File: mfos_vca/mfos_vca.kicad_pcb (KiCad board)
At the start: 2 copper layers, 236.8 x 141.5 mm, 89 parts, among them J1 CV1 A, J2 CV2 A, J3 Signal In A, J4 Signal Out A, J5 CV1 B, J6 CV2 B, J7 Signal In B, J8 Signal Out A, J9 Conn_02x05_Odd_Even, Q1 2N3904, Q2 2N3906, Q3 2N3904, Q4 2N3906, SW1 SW_SPDT, SW2 SW_SPDT, U1 TL074, U2 LM13700

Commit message: Remove secondary CV input per VCA, some more panel progress
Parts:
- J1: renamed from J2; footprint Connector_PinHeader_2.54mm:PinHeader_1x03_P2.54mm_Vertical_AudioJack -> Connector_PinHeader_2.54mm:PinHeader_1x03_P2.54mm_Vertical
- J2: renamed from J3; footprint Connector_PinHeader_2.54mm:PinHeader_1x03_P2.54mm_Vertical_AudioJack -> Connector_PinHeader_2.54mm:PinHeader_1x03_P2.54mm_Vertical
- J3: renamed from J4; footprint Connector_PinHeader_2.54mm:PinHeader_1x03_P2.54mm_Vertical_AudioJack -> Connector_PinHeader_2.54mm:PinHeader_1x03_P2.54mm_Vertical
- J4: renamed from J6; footprint Connector_PinHeader_2.54mm:PinHeader_1x03_P2.54mm_Vertical_AudioJack -> Connector_PinHeader_2.54mm:PinHeader_1x03_P2.54mm_Vertical
- J5: renamed from J7; footprint Connector_PinHeader_2.54mm:PinHeader_1x03_P2.54mm_Vertical_AudioJack -> Connector_PinHeader_2.54mm:PinHeader_1x03_P2.54mm_Vertical
- J6: renamed from J8; footprint Connector_PinHeader_2.54mm:PinHeader_1x03_P2.54mm_Vertical_AudioJack -> Connector_PinHeader_2.54mm:PinHeader_1x03_P2.54mm_Vertical
- J7: renamed from J9; moved to B.Cu
- moved J7 140.9 mm to (275.5, 129.5), turned to 180 degrees
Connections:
- R13 pad 1: Net-(J3-PadT) -> Net-(J2-PadT)
- R19 pad 2: Net-(J4-PadT) -> Net-(J3-PadT)
- R2 pad 1: Net-(J2-PadT) -> Net-(J1-PadT)
- R20 pad 1: Net-(J6-PadT) -> Net-(J4-PadT)
- R24 pad 1: Net-(J7-PadT) -> Net-(J5-PadT)
- R38 pad 2: Net-(J8-PadT) -> Net-(J6-PadT)
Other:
- outline, holes or cut-outs redrawn
- board text added: "CV"
- board text added: "IN"
- board text added: "LIN"
- board text added: "LOG"
- board text added: "OFFSET"
- board text added: "OUT"
- board text removed: "OFFSET A"

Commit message: More progress, got rid of second cv input
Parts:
- removed the J1 at (30.0, 65.0)
- removed the J1 at (29.0, 83.0)
- removed R1: 100k, Resistor_THT:R_Axial_DIN0207_L6.3mm_D2.5mm_P10.16mm_Horizontal
- added J1: CV A, Library:PinHeader_1x03_P2.54mm_Vertical_AudioJack, F.Cu at (244.4, 76.4)
- added REF**: MountingHole_3.2mm_M3, MountingHole:MountingHole_3.2mm_M3, F.Cu at (212.5, 147.5)
- added REF**: MountingHole_3.2mm_M3, MountingHole:MountingHole_3.2mm_M3, F.Cu at (212.5, 36.0)
- added REF**: MountingHole_3.2mm_M3, MountingHole:MountingHole_3.2mm_M3, F.Cu at (333.9, 150.0)
- added REF**: MountingHole_3.2mm_M3, MountingHole:MountingHole_3.2mm_M3, F.Cu at (308.5, 150.0)
- added REF**: MountingHole_3.2mm_M3, MountingHole:MountingHole_3.2mm_M3, F.Cu at (308.5, 49.5)
- added REF**: MountingHole_3.2mm_M3, MountingHole:MountingHole_3.2mm_M3, F.Cu at (212.5, 158.5)
- added REF**: MountingHole_3.2mm_M3, MountingHole:MountingHole_3.2mm_M3, F.Cu at (212.5, 47.0)
- added REF**: MountingHole_3.2mm_M3, MountingHole:MountingHole_3.2mm_M3, F.Cu at (333.9, 49.5)
- J2, J3, J5: footprint Connector_PinHeader_2.54mm:PinHeader_1x03_P2.54mm_Vertical -> Library:PinHeader_1x03_P2.54mm_Vertical_AudioJack
- J4: value CV2 B -> CV B; footprint Connector_PinHeader_2.54mm:PinHeader_1x03_P2.54mm_Vertical -> Library:PinHeader_1x03_P2.54mm_Vertical_AudioJack
- J6: value Signal Out A -> Signal Out B; footprint Connector_PinHeader_2.54mm:PinHeader_1x03_P2.54mm_Vertical -> Library:PinHeader_1x03_P2.54mm_Vertical_AudioJack
- RV2, RV3: moved to B.Cu
- moved REF** 268.2 mm to (201.8, -133.0)
- moved REF** 268.2 mm to (201.8, -122.0)
- moved REF** 268.2 mm to (201.8, -10.5)
- moved REF** 268.2 mm to (201.8, -21.5)
- moved REF** 268.2 mm to (176.4, -10.5)
- moved REF** 268.2 mm to (176.4, -133.0)
- moved REF** 268.2 mm to (176.4, -122.0)
- moved REF** 268.2 mm to (176.4, -21.5)
- moved J3 244.3 mm to (287.5, 66.5)
- moved U2 215.3 mm to (257.0, 101.0), turned to 90 degrees
- moved J2 211.7 mm to (244.4, 66.0)
- moved R4 211.0 mm to (247.8, 63.5)
- moved R2 210.8 mm to (247.8, 59.5)
- moved SW1 210.5 mm to (287.5, 55.9)
- moved R3 203.2 mm to (247.9, 55.0)
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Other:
- board size 236.8 x 141.5 mm -> 196.4 x 297.5 mm

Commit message: vca pcb progress from last night
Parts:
- moved R2 19.4 mm to (258.8, 43.5)
- moved R12 18.1 mm to (272.0, 58.5), turned to 90 degrees
- moved R7 13.1 mm to (252.0, 58.7), turned to 90 degrees
- moved R6 13.0 mm to (248.0, 58.5), turned to 90 degrees
- moved R11 13.0 mm to (268.0, 58.5), turned to 90 degrees
- moved R3 11.9 mm to (244.8, 43.5)
- moved C1 10.1 mm to (244.5, 138.5)
- moved C2 10.1 mm to (244.5, 129.0)
- moved C3 10.1 mm to (243.5, 121.5)
- moved C4 10.1 mm to (243.5, 116.0)
- moved D1 10.1 mm to (267.5, 141.0)
- moved D2 10.1 mm to (263.0, 133.4)
- moved J1 10.1 mm to (235.9, 70.9)
- moved J3 10.1 mm to (279.0, 61.0)
- moved J7 10.1 mm to (277.0, 123.8)
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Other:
- outline, holes or cut-outs redrawn

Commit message: Finished placing components on vca board
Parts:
- removed the J4 at (114.2, 97.2)
- removed the REF** at (333.9, 150.0)
- removed the REF** at (308.5, 150.0)
- removed the REF** at (308.5, 49.5)
- removed the REF** at (333.9, 49.5)
- J4: renamed from J5; value CV1 B -> CV B
- RV5, RV6: moved to B.Cu
- moved R27 159.4 mm to (269.1, 116.7), turned to 90 degrees
- moved R26 156.8 mm to (265.1, 116.7), turned to 90 degrees
- moved R25 154.4 mm to (261.1, 116.7), turned to 90 degrees
- moved R37 153.5 mm to (268.9, 131.2), turned to 90 degrees
- moved R36 151.7 mm to (264.8, 131.2), turned to 90 degrees
- moved R24 151.4 mm to (257.0, 114.7), turned to 90 degrees
- moved R38 151.2 mm to (274.5, 114.7), turned to 90 degrees
- moved R35 150.1 mm to (260.8, 131.2), turned to 90 degrees
- moved R23 149.4 mm to (252.9, 114.7), turned to 90 degrees
- moved R34 147.2 mm to (256.7, 128.2), turned to 90 degrees
- moved R22 146.7 mm to (249.0, 114.7), turned to 90 degrees
- moved R28 146.5 mm to (260.5, 103.0)
- moved J6 144.8 mm to (279.0, 104.4)
- moved R21 143.4 mm to (245.0, 114.5), turned to 90 degrees
- moved R20 140.3 mm to (241.0, 114.5), turned to 90 degrees
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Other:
- board size 196.4 x 297.5 mm -> 168.8 x 292 mm

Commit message: Almost done all of the tracks in vca pcb, fix the custom library footprint
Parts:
- removed the REF** at (176.4, -133.0)
- removed the REF** at (176.4, -122.0)
- removed the REF** at (201.8, -122.0)
- removed the REF** at (201.8, -10.5)
- removed the REF** at (201.8, -21.5)
- removed the REF** at (176.4, -21.5)
- removed the REF** at (201.8, -133.0)
- removed the REF** at (176.4, -10.5)
- J1, J2, J3, J5, J6: footprint Library:PinHeader_1x03_P2.54mm_Vertical_AudioJack -> CustomStuff:PinHeader_1x03_P2.54mm_Vertical_AudioJack
- J4: footprint Connector_PinHeader_2.54mm:PinHeader_1x03_P2.54mm_Vertical_AudioJack -> CustomStuff:PinHeader_1x03_P2.54mm_Vertical_AudioJack
- moved Q3 46.5 mm to (219.6, 97.2)
- moved Q4 46.5 mm to (226.1, 97.2)
- moved C7 45.2 mm to (236.1, 90.7)
- moved Q2 42.8 mm to (233.6, 97.2)
- moved R3 40.0 mm to (201.6, 61.7)
- moved R13 40.0 mm to (201.6, 64.6)
- moved R6 40.0 mm to (209.6, 61.6)
- moved R15 40.0 mm to (205.6, 74.7)
- moved R16 40.0 mm to (209.6, 74.7)
- moved R5 40.0 mm to (205.7, 61.7)
- moved RV6 39.6 mm to (214.6, 101.7), turned to -90 degrees
- moved J4 39.1 mm to (197.0, 101.0)
- moved R4 39.1 mm to (214.7, 61.7)
- moved C2 39.1 mm to (207.1, 136.7)
- moved C8 39.1 mm to (221.6, 90.7)
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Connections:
- J4 pad T: Net-(J5-PadT) -> Net-(J4-PadT)
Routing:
- net -12V: track 0.00 -> 286.3 mm
- net +12V: track 0.00 -> 259.6 mm
- net Net-(R25-Pad2): track 0.00 -> 90.6 mm, vias 0 -> 1
- net Net-(U1C--): track 0.00 -> 84.3 mm, vias 0 -> 2
- net Net-(Q1-B): track 0.00 -> 82.2 mm, vias 0 -> 3
- net Net-(Q3-B): track 0.00 -> 67.1 mm, vias 0 -> 3
- net Net-(U1C-+): track 0.00 -> 62.2 mm, vias 0 -> 1
- net GND: track 0.00 -> 61.5 mm, vias 0 -> 4
- net Net-(Q3-E): track 0.00 -> 57.7 mm, vias 0 -> 2
- net Net-(U1D--): track 0.00 -> 54.6 mm, vias 0 -> 2
- net Net-(R36-Pad2): track 0.00 -> 53.1 mm, vias 0 -> 1
- net Net-(R37-Pad2): track 0.00 -> 52.6 mm, vias 0 -> 1
- net Net-(U1D-+): track 0.00 -> 51.5 mm, vias 0 -> 1
- net Net-(SW2-C): track 0.00 -> 47.9 mm
- net Net-(Q2-C): track 0.00 -> 47.7 mm, vias 0 -> 1
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- added copper zone on B.Cu, net GND
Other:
- board size 168.8 x 292 mm -> 129.9 x 128.5 mm
- board text removed: "COARSE"
- board text removed: "FINE"
- board text removed: "FM"
- board text removed: "FM LEVEL"
- board text removed: "MK VCO"
- board text removed: "PULSE"
- board text removed: "PULSE WIDTH"
- board text removed: "PWM"
- board text removed: "PWM LEVEL"
- board text removed: "SAW"
- board text removed: "V/OCT"

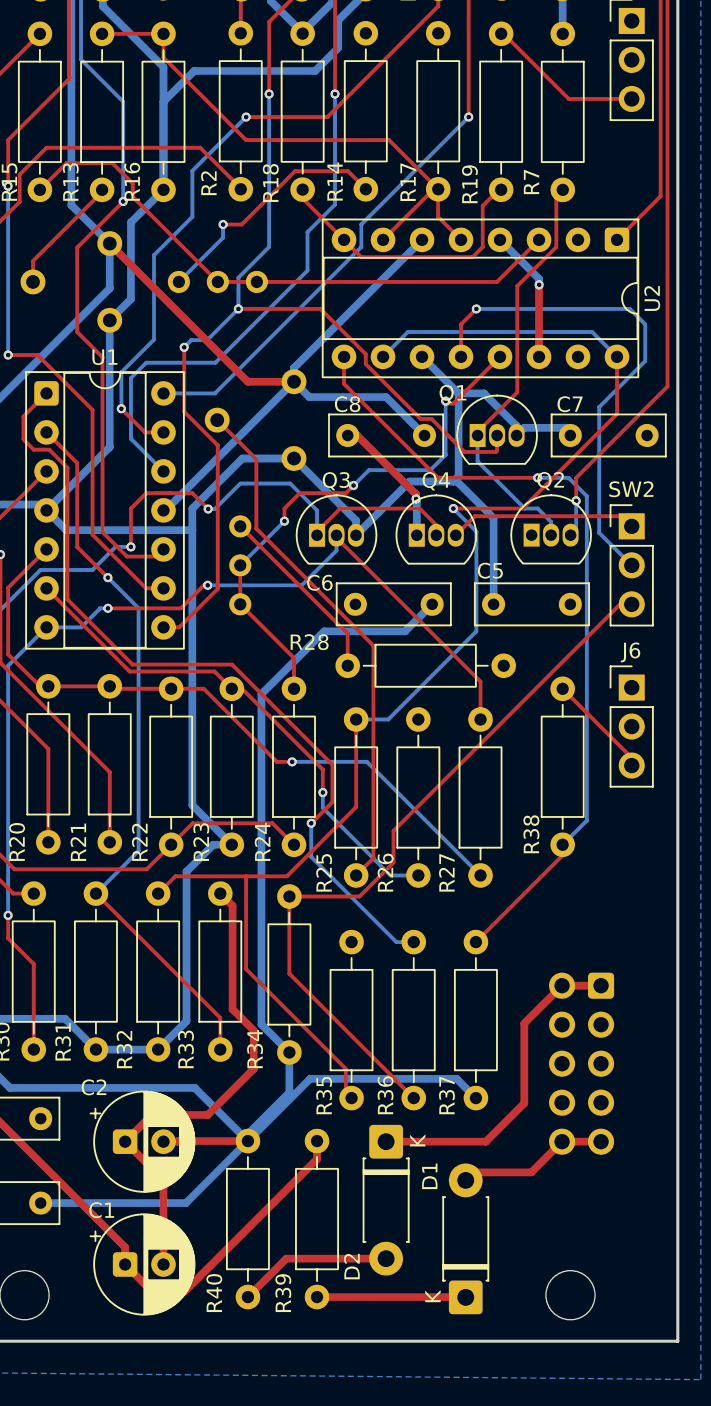
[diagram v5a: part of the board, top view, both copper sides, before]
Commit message: All DRC errors resolved :)
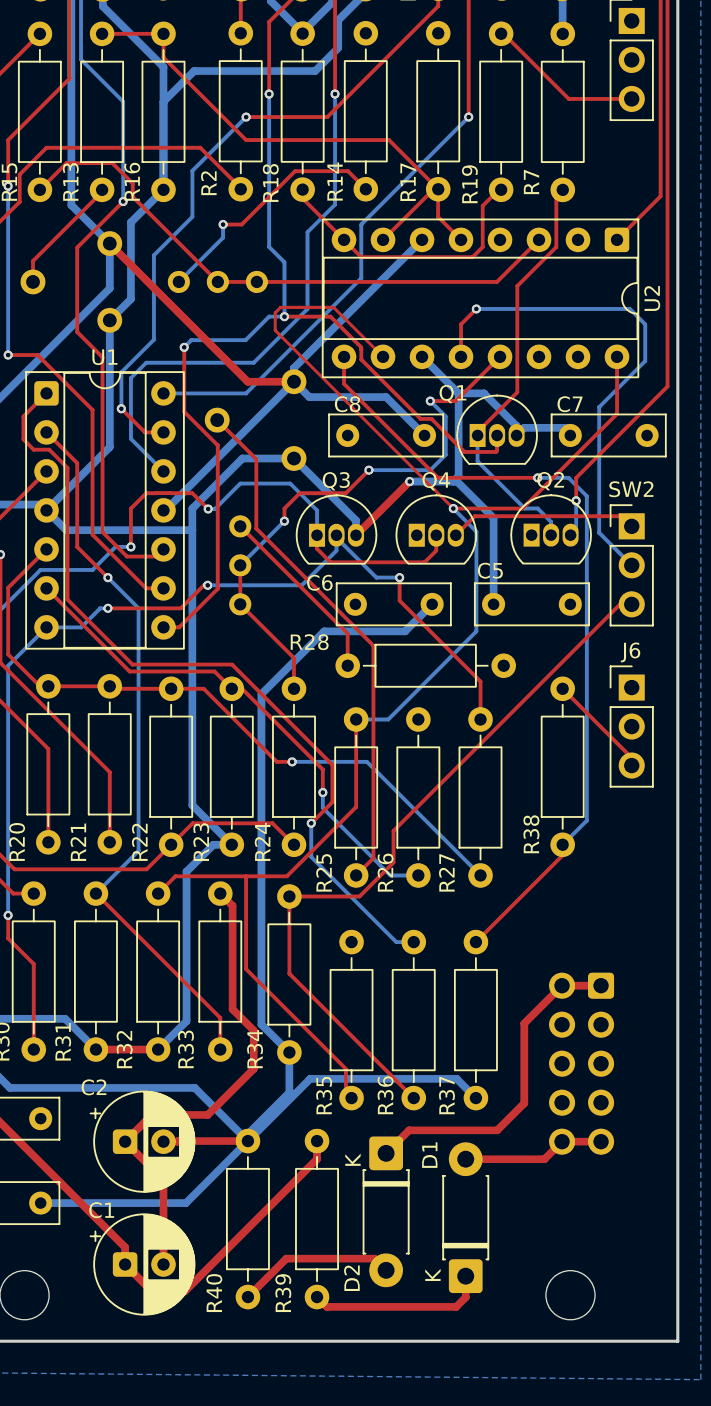
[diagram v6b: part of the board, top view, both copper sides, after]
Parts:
- moved D1 1.38 mm to (229.3, 145.5)
- moved D2 0.76 mm to (224.1, 137.5)
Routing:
- net GND: track 61.5 -> 44.1 mm, vias 4 -> 2
- net Net-(R25-Pad2): track 90.6 -> 100.0 mm
- net Net-(D1-K): track 9.70 -> 11.6 mm
- net Net-(U1D-+): track 51.5 -> 52.9 mm
- net Net-(U2A--): track 34.7 -> 36.0 mm
- net Net-(R11-Pad2): track 47.6 -> 48.8 mm
- net Net-(Q3-B): track 67.1 -> 68.1 mm, vias 3 -> 4
- net Net-(Q3-E): track 57.7 -> 58.3 mm
- net Net-(D1-A): track 9.86 -> 9.29 mm
- net +12V: vias 0 -> 1

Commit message: Finalize panel and pcb for VCA, add gerbers
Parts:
- removed the REF** at (156.2, 142.0)
- removed the REF** at (156.2, 153.0)
- removed the REF** at (156.2, 41.5)
- removed the REF** at (120.8, 142.0)
- removed the REF** at (120.8, 30.5)
- removed the REF** at (156.2, 30.5)
- removed the REF** at (120.8, 153.0)
- removed the REF** at (120.8, 41.5)
- moved R13 73.6 mm to (127.9, 65.0)
- moved C1 73.6 mm to (133.5, 145.2)
- moved C2 73.6 mm to (133.5, 137.2)
- moved C3 73.6 mm to (123.0, 135.7)
- moved C4 73.6 mm to (123.0, 141.2)
- moved C5 73.6 mm to (157.5, 102.2)
- moved C6 73.6 mm to (148.5, 102.2)
- moved C7 73.6 mm to (162.5, 91.2)
- moved C8 73.6 mm to (148.0, 91.2)
- moved D1 73.6 mm to (155.7, 145.9)
- moved D2 73.6 mm to (150.5, 137.9)
- moved J3 73.6 mm to (166.5, 64.2)
- moved J4 73.6 mm to (123.4, 101.4)
- moved J5 73.6 mm to (123.5, 111.5)
- moved J6 73.6 mm to (166.5, 107.6)
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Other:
- board size 129.9 x 128.5 mm -> 49.5 x 106.5 mm
- board text added: "LM13700 VCA Jesse Holzman"
- board text removed: "CV"
- board text removed: "IN"
- board text removed: "LIN"
- board text removed: "LOG"
- board text removed: "OFFSET"
- board text removed: "OUT"

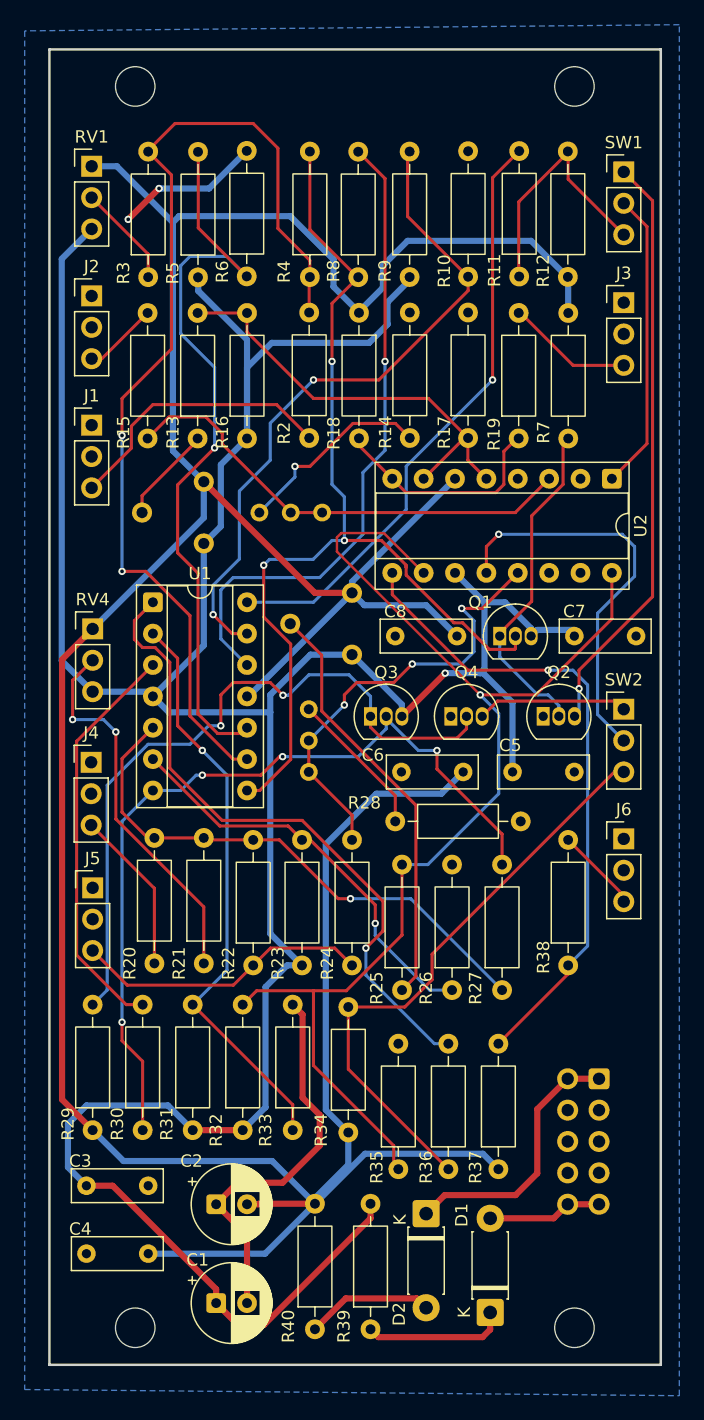
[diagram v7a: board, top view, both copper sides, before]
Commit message: fix a couple stupid mistakes in schematic
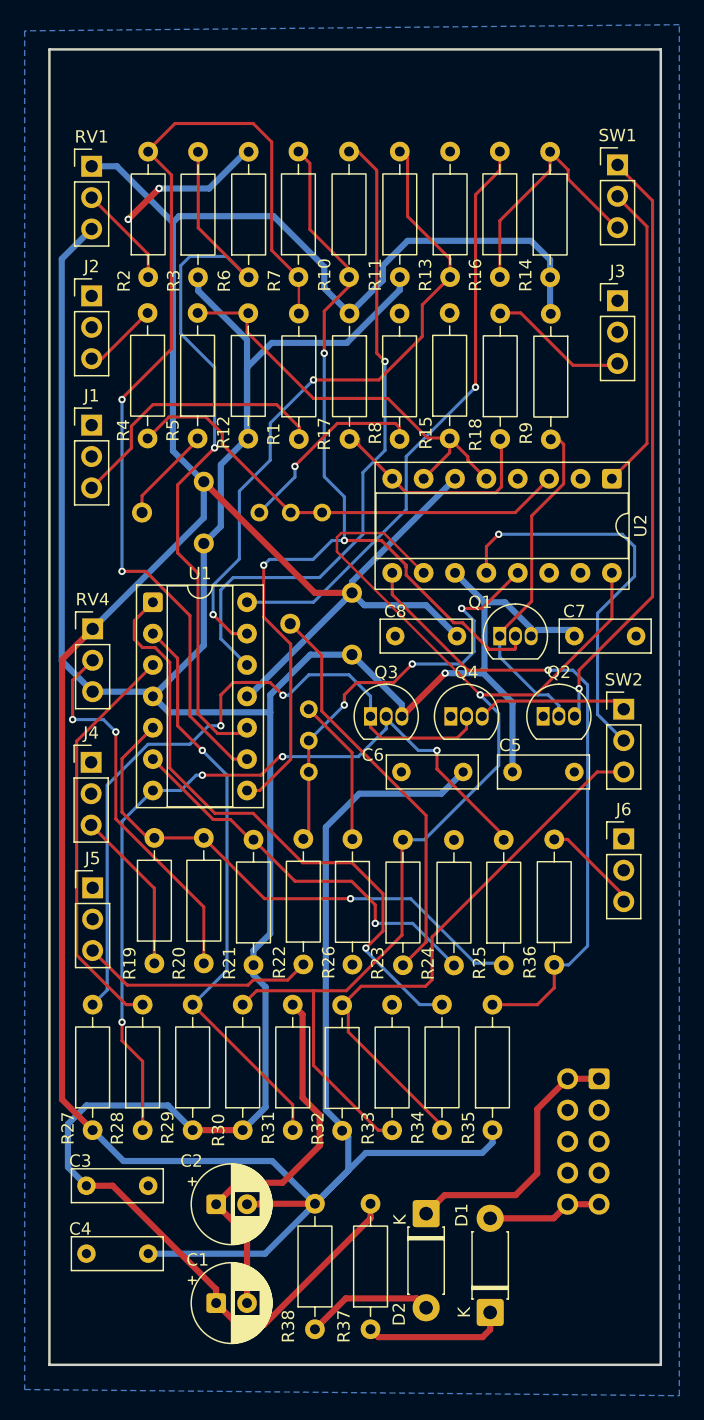
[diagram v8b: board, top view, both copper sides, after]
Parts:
- removed the R22 at (136.5, 117.8)
- removed REF** (x4): MountingHole_3.2mm_M3, MountingHole:MountingHole_3.2mm_M3
- moved R22 3.94 mm to (140.6, 117.7)
- moved R21 3.92 mm to (136.5, 117.8)
- moved R26 3.75 mm to (144.5, 107.6), turned to -90 degrees
- moved R34 3.20 mm to (151.8, 131.1)
- moved R35 3.19 mm to (155.9, 131.2)
- moved R33 3.19 mm to (147.7, 131.2)
- moved R23 2.01 mm to (148.6, 117.8)
- moved R25 2.00 mm to (156.8, 117.8)
- moved R24 2.00 mm to (152.8, 117.8)
- moved R16 1.57 mm to (156.5, 62.1)
- moved R18 1.49 mm to (156.5, 75.2)
- moved R15 1.49 mm to (152.4, 75.2)
- moved R13 1.46 mm to (152.4, 62.1)
- moved R14 1.44 mm to (160.5, 62.1)
- moved R9 1.41 mm to (160.6, 65.1)
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- renumbered R2 to R1, R8 to R10, R9 to R11, R16 to R12, R10 to R13, R12 to R14, R17 to R15, R11 to R16, R18 to R17, R19 to R18, R20 to R19, R3 to R2, R21 to R20, R23 to R21, R24 to R22, R25 to R23, R26 to R24, R27 to R25, R28 to R26, R29 to R27, R30 to R28, R31 to R29, R5 to R3, R32 to R30, R33 to R31, R34 to R32, R35 to R33, R36 to R34, R37 to R35, R38 to R36, R39 to R37, R40 to R38, R13 to R4, R15 to R5, R4 to R7, R14 to R8, R7 to R9, RV3 to RV2, RV2 to RV3
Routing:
- net Net-(J5-PadT): track 24.0 -> 18.9 mm
- net Net-(R23-Pad2): track 100.0 -> 97.1 mm
- net +12V: track 259.6 -> 256.7 mm
- net Net-(R34-Pad2): track 53.1 -> 51.0 mm
- net Net-(SW2-C): track 47.9 -> 46.1 mm
- net Net-(Q3-B): track 68.1 -> 66.4 mm
- net Net-(R12-Pad2): track 36.0 -> 34.3 mm
- net Net-(R23-Pad1): track 34.3 -> 33.0 mm
- net Net-(U2A--): track 36.0 -> 34.6 mm
- net Net-(U1B--): track 33.4 -> 32.2 mm
- net Net-(J6-PadT): track 6.86 -> 8.01 mm
- net Net-(J3-PadT): track 10.3 -> 11.3 mm
- net Net-(U1D--): track 54.6 -> 53.8 mm
- net Net-(Q2-C): track 47.7 -> 48.4 mm
- net Net-(SW1-B): track 24.3 -> 25.0 mm
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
